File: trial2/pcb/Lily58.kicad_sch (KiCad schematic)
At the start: 114 parts, among them P3 ICSP, P4 OLED, SW1 SW_PUSH, SW10 SW_PUSH, SW11 SW_PUSH, SW12 SW_PUSH, SW13 SW_PUSH, SW14 SW_PUSH, SW15 SW_PUSH, SW16 SW_PUSH, SW17 SW_PUSH, SW18 SW_PUSH, SW19 SW_PUSH, SW2 SW_PUSH, SW20 SW_PUSH, SW21 SW_PUSH, SW22 SW_PUSH, SW23 SW_PUSH, SW24 SW_PUSH, SW25 Rotary_Encoder_Switch, SW26 SW_PUSH, SW27 SW_PUSH, SW28 SW_PUSH, SW29 SW_PUSH, SW3 SW_PUSH, SW4 SW_PUSH, SW5 SW_PUSH, SW6 SW_PUSH, SW7 SW_PUSH, SW8 SW_PUSH, SW9 SW_PUSH, U1 NiceNano

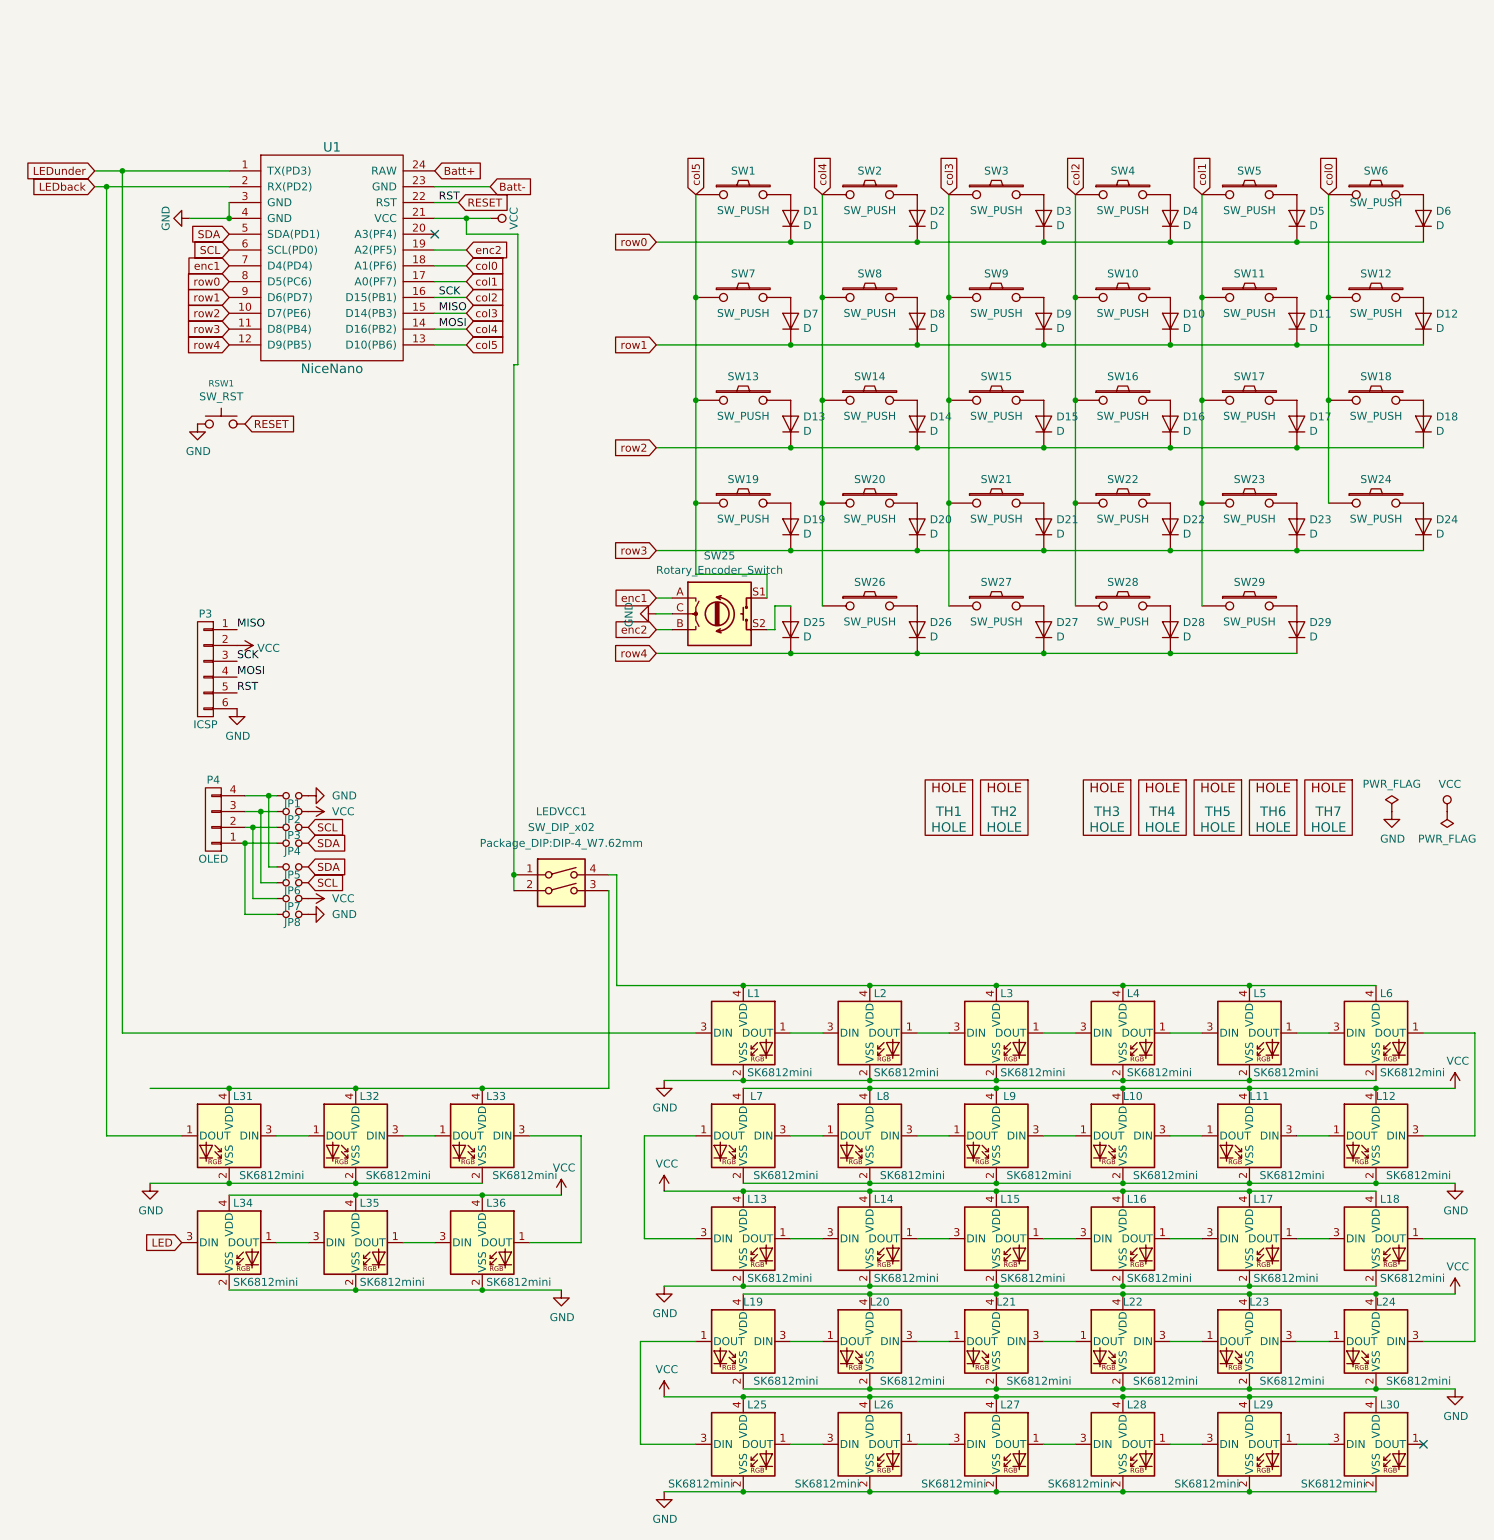
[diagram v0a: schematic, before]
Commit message: Add libraries, new design
Turns out DIP switches aren't rated for the LED current, so I need a SPDT switch with a diode placed in between. This means you can have the backlight on, none on, or the backlight and underglow on. I might reverse this decision later on. Who knows
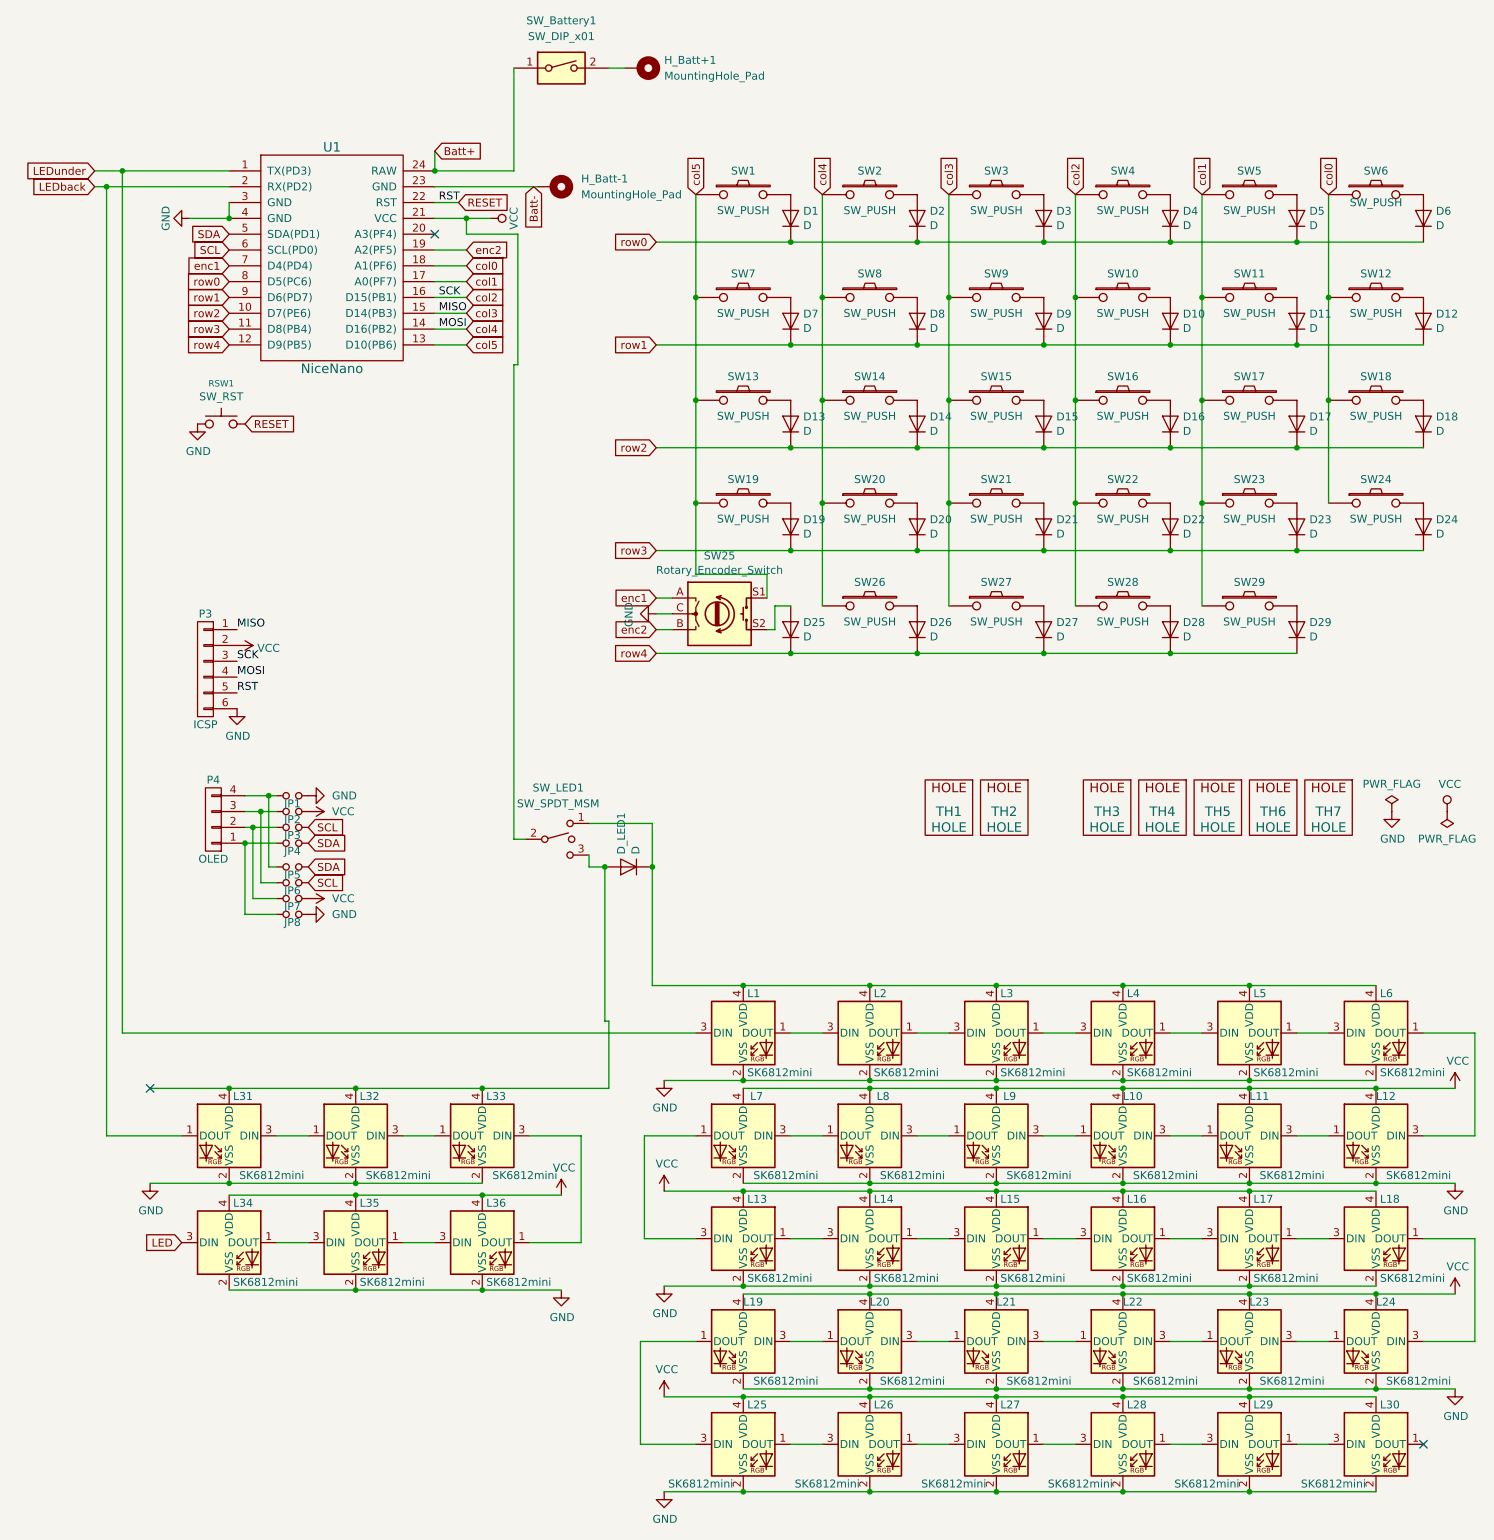
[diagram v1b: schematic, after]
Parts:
- removed LEDVCC1: SW_DIP_x02, Package_DIP:DIP-4_W7.62mm, symbol Switch:SW_DIP_x02
- added D_LED1: D, Diode_THT:D_A-405_P7.62mm_Horizontal, symbol Lily58-rescue:D-Lily58-cache
- added H_Batt+1, H_Batt-1: MountingHole_Pad, MountingHole:MountingHole_2.1mm, symbol Mechanical:MountingHole_Pad
- added SW_Battery1: SW_DIP_x01, Button_Switch_THT:SW_CuK_OS102011MA1QN1_SPDT_Angled, symbol Switch:SW_DIP_x01
- added SW_LED1: SW_SPDT_MSM, symbol Switch:SW_SPDT_MSM
- D1, D10, D11, D12, D13, D14, D15, D16, D17, D18, D19, D2, D20, D21, D22, D23, D24, D25, D26, D27, D28, D29, D3, D4, D5, D6, D7, D8, D9: footprint Lily58-footprint:Diode_TH_SOD123 -> Diode_THT:D_A-405_P7.62mm_Horizontal
- L1, L10, L11, L12, L13, L14, L15, L16, L17, L18, L19, L2, L20, L21, L22, L23, L24, L25, L26, L27, L28, L29, L3, L30, L4, L5, L6, L7, L8, L9: footprint Lily58-footprint:SK6812MINI_rev -> LED_SMD:LED_SK6812MINI_PLCC4_3.5x3.5mm_P1.75mm
- L31, L32, L33, L34, L35, L36: footprint Lily58-footprint:SK6812MINI_underglow_rev -> LED_SMD:LED_SK6812MINI_PLCC4_3.5x3.5mm_P1.75mm
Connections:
- net Batt+: now also SW_Battery1.1
- net Batt-: now also H_Batt-1.1
- net VCC: now also SW_LED1.2
- net at L1.4 (VDD), L2.4 (VDD), L3.4 (VDD)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: now also D_LED1.1 (K), SW_LED1.1
- net at L31.4 (VDD), L32.4 (VDD), L33.4 (VDD): now also D_LED1.2 (A), SW_LED1.3
- new net: H_Batt+1.1, SW_Battery1.2
- no-connect marks 2 -> 3
